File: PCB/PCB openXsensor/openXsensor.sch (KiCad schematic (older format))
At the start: 32 parts, among them P1 Digital, P10 VFAS/COURANT, P11 GY-86, P12 NTC1, P13 NTC2, P14 ALIM, P16 4S, P17 ADS1115, P18 ADS_IN, P2 Analog, P3 ADC, P4 ADC, P4-2 ADC, P5 GPS, P6 HUB/SPORT, P7 PPM, P8 FUEL, P9 RPM

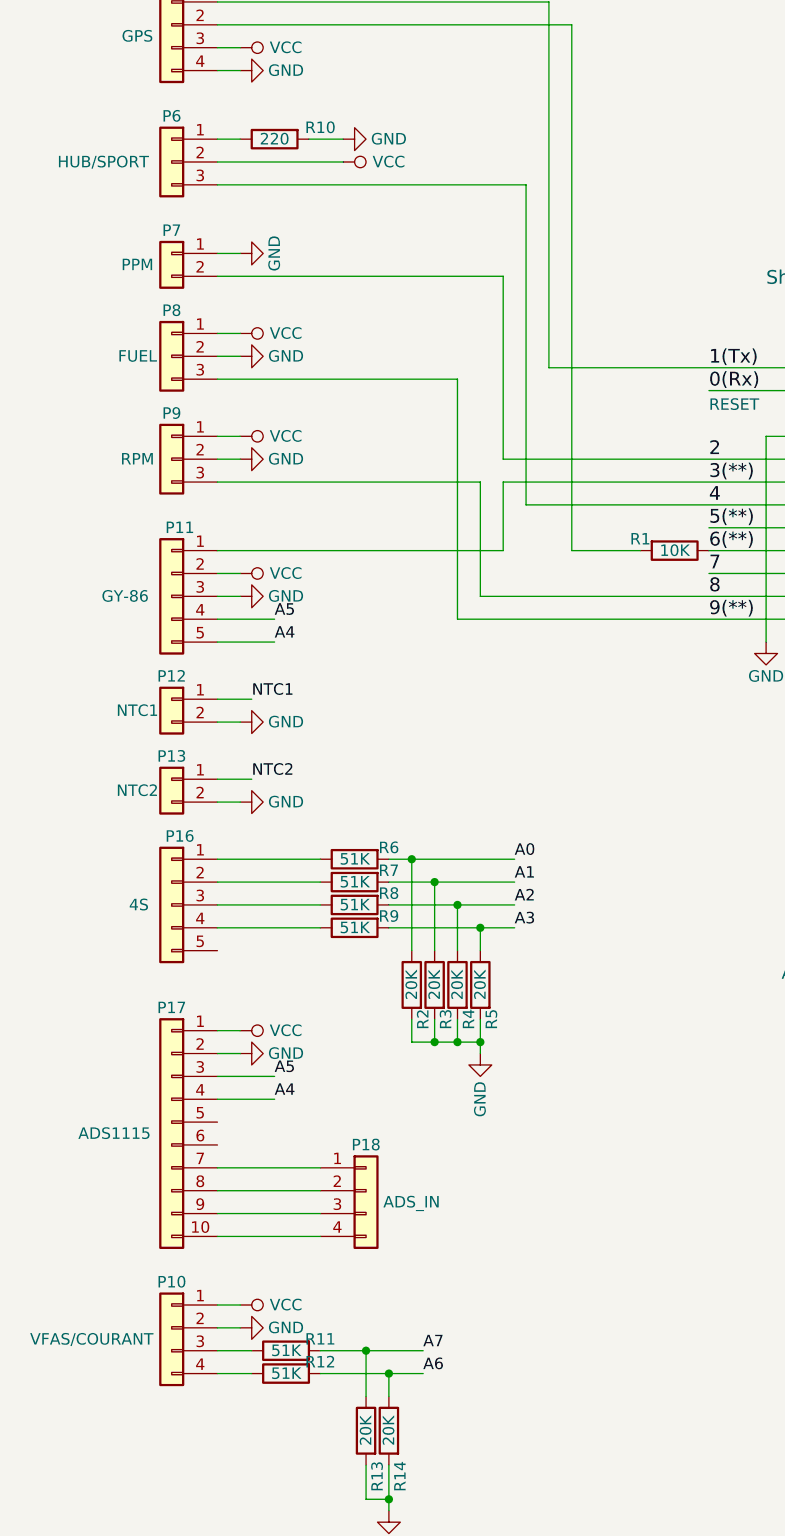
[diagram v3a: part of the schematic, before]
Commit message: Update oXs pcb
Move connectors p8 p9 under pro mini
Add connector between 5v and sport connector. 
Add gnd ads1115 addr pin (0x48).
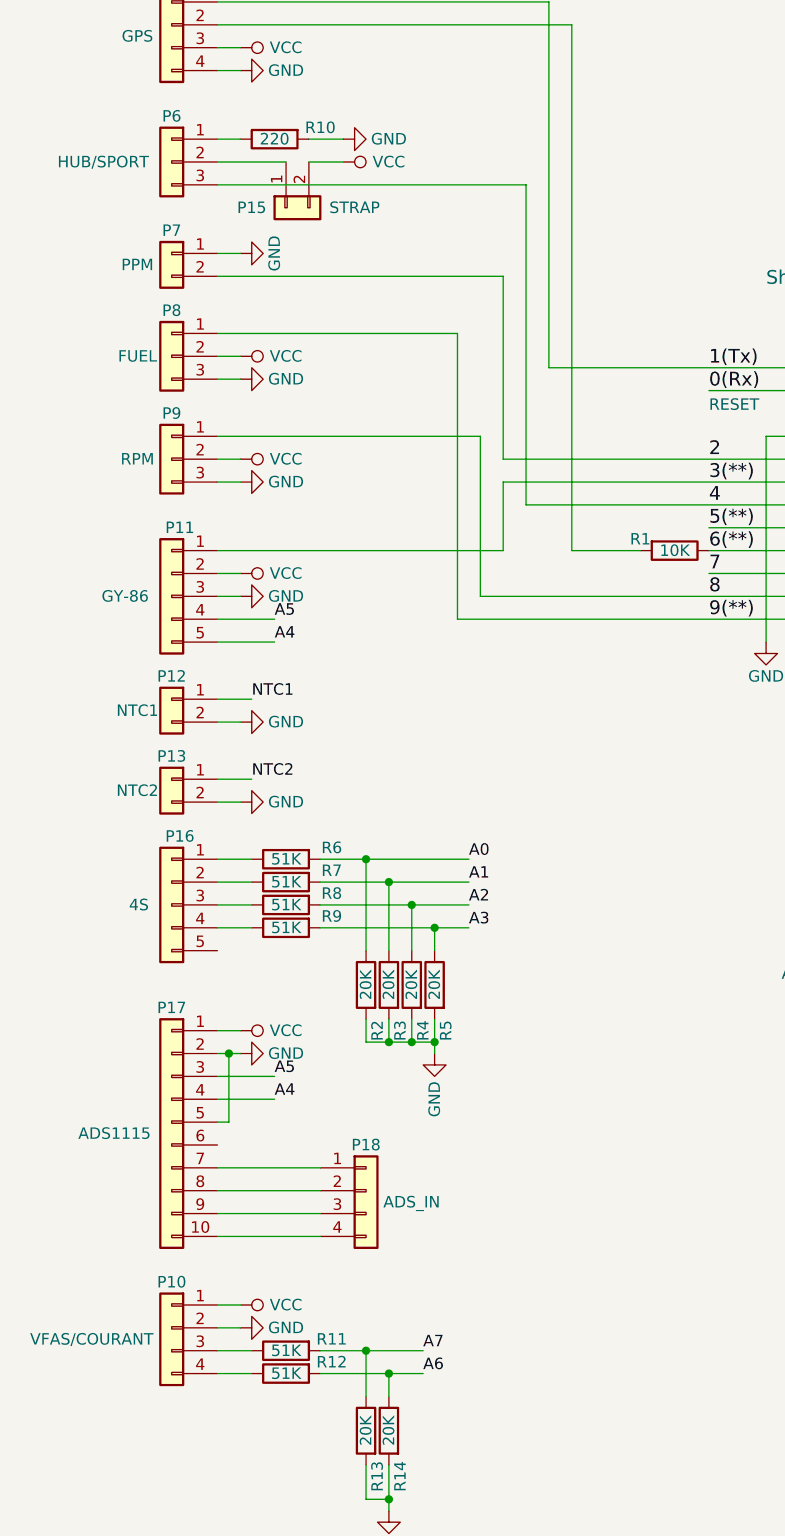
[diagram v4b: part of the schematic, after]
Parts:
- added P15: STRAP, Pin_Header_Straight_1x02_Pitch2.54mm, symbol Connector_Generic:Conn_01x02
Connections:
- net 8: now also P9.1 (Pin_1); no longer P9.3 (Pin_3)
- net 9(**): now also P8.1 (Pin_1); no longer P8.3 (Pin_3)
- net GND: now also P17.5 (Pin_5), P8.3 (Pin_3), P9.3 (Pin_3); no longer P8.2 (Pin_2), P9.2 (Pin_2)
- net VCC: now also P8.2 (Pin_2), P9.2 (Pin_2), P15.2 (Pin_2); no longer P6.2 (Pin_2), P8.1 (Pin_1), P9.1 (Pin_1)
- new net: P15.1 (Pin_1), P6.2 (Pin_2)
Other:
- moved on the sheet: R2, R3, R4, R5, R6, R7, R8, R9

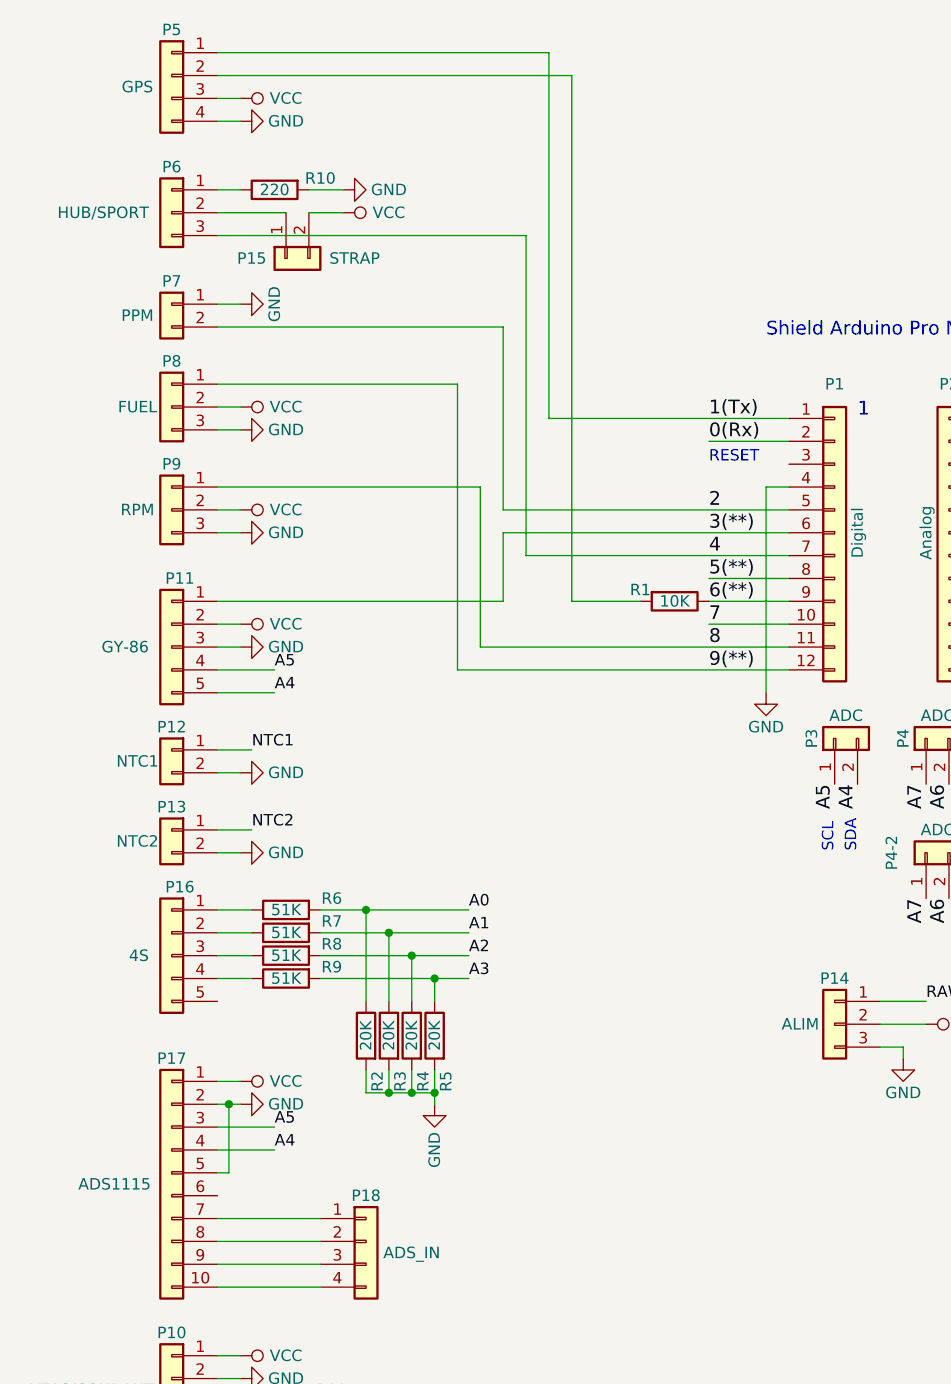
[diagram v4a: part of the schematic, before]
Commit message: Update pcb oxs
Change wire on gps connector
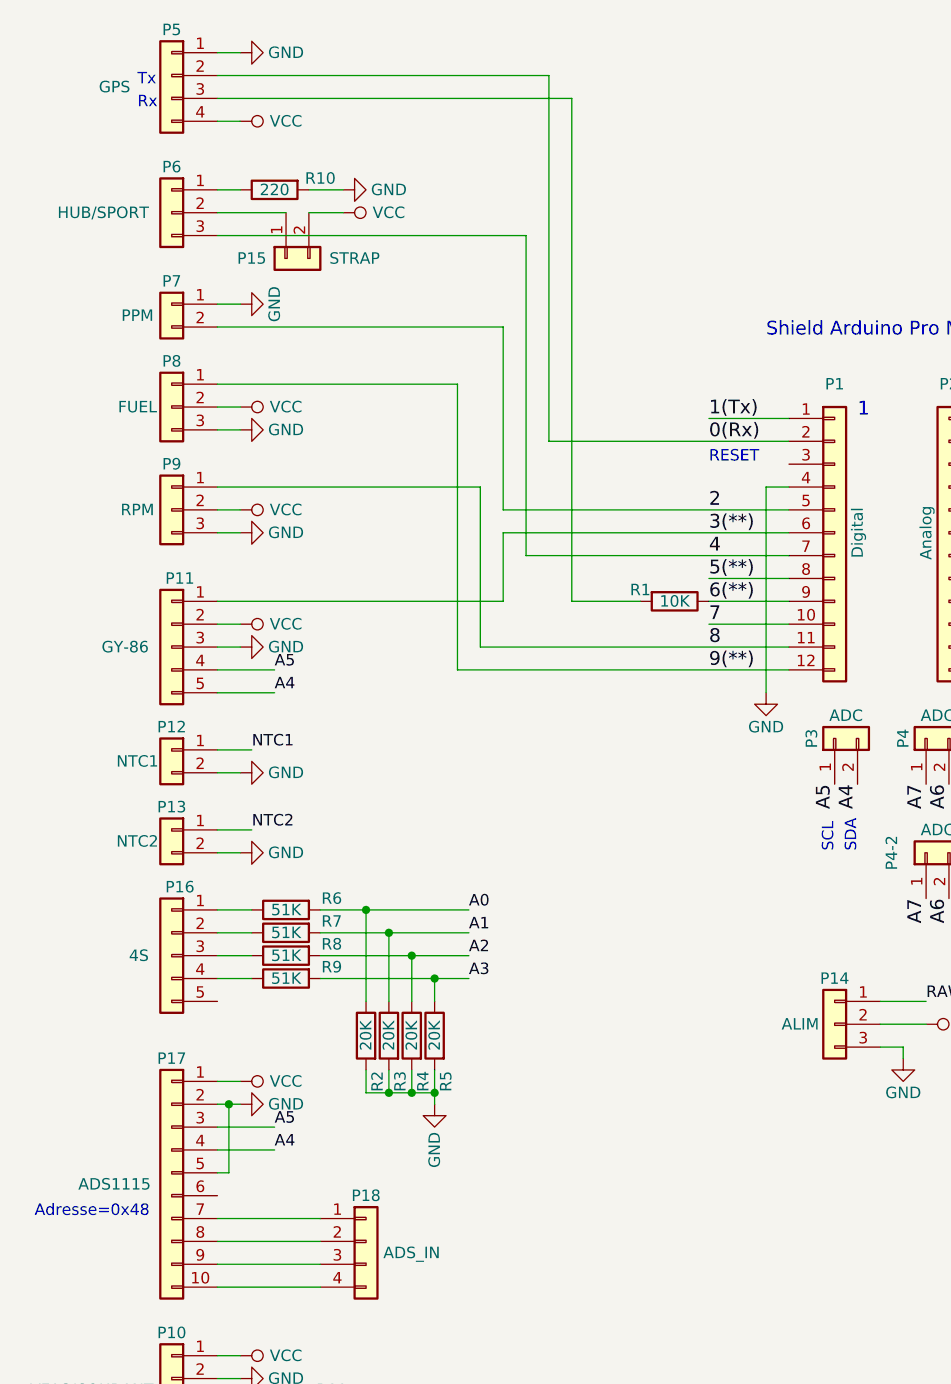
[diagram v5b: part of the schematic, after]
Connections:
- net 0(Rx): now also P5.2 (Pin_2)
- net 1(Tx): no longer P5.1 (Pin_1)
- net GND: now also P5.1 (Pin_1); no longer P5.4 (Pin_4)
- net VCC: now also P5.4 (Pin_4); no longer P5.3 (Pin_3)
- net at R1.2: now also P5.3 (Pin_3); no longer P5.2 (Pin_2)
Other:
- note added: "Adresse=0x48"
- note added: "Rx"
- note added: "Tx"
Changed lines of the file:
@@
 Sheet 1 1
 Title ""
-Date "2019-10-07"
+Date "2019-10-12"
 Rev ""
 Comp ""
@@
 	5450 2600 5450 3500
 Wire Wire Line
-	5200 2400 5550 2400
-Wire Wire Line
 	5200 3000 5550 3000
 Wire Wire Line
@@
 P 2850 800
 F 0 "P5" H 2850 1000 50  0000 C CNN
-F 1 "GPS" H 3000 750 50  0000 C CNN
+F 1 "GPS" H 3100 750 50  0000 C CNN
 F 2 "Pin_Header_Straight_1x04_Pitch2.54mm" H 2850 800 50  0001 C CNN
 F 3 "~" H 2850 800 50  0001 C CNN
@@
 	4900 3100 4600 3100
 Wire Wire Line
-	4600 3100 4600 800
-Wire Wire Line
-	4600 800  3050 800
-Wire Wire Line
-	4500 2300 5550 2300
-Wire Wire Line
-	3050 1000 3150 1000
+	4600 3100 4600 900
+Wire Wire Line
+	3050 700  3150 700
 $Comp
 L power:GND #PWR0101
 U 1 1 5D744512
-P 3150 1000
-F 0 "#PWR0101" H 3150 750 50  0001 C CNN
-F 1 "GND" V 3150 800 50  0000 C CNN
-F 2 "" H 3150 1000 50  0000 C CNN
-F 3 "" H 3150 1000 50  0000 C CNN
-	1    3150 1000
+P 3150 700
+F 0 "#PWR0101" H 3150 450 50  0001 C CNN
+F 1 "GND" V 3150 500 50  0000 C CNN
+F 2 "" H 3150 700 50  0000 C CNN
+F 3 "" H 3150 700 50  0000 C CNN
+	1    3150 700
 	0    -1   -1   0
 $EndComp
@@
 L power:VCC #PWR0104
 U 1 1 5D746203
-P 3150 900
-F 0 "#PWR0104" H 3150 750 50  0001 C CNN
-F 1 "VCC" V 3150 1100 50  0000 C CNN
-F 2 "" H 3150 900 50  0000 C CNN
-F 3 "" H 3150 900 50  0000 C CNN
-	1    3150 900
+P 3150 1000
+F 0 "#PWR0104" H 3150 850 50  0001 C CNN
+F 1 "VCC" V 3150 1200 50  0000 C CNN
+F 2 "" H 3150 1000 50  0000 C CNN
+F 3 "" H 3150 1000 50  0000 C CNN
+	1    3150 1000
 	0    1    1    0
 $EndComp
@@
 	3050 2800 3150 2800
 Wire Wire Line
-	3150 900  3050 900
-Wire Wire Line
-	4500 700  3050 700
+	3150 1000 3050 1000
 $Comp
 L Connector_Generic:Conn_01x04 P18
@@
 Wire Wire Line
 	4400 1500 4400 2900
-Wire Wire Line
-	4500 700  4500 2300
 $Comp
 L Device:R R14
@@
 Wire Wire Line
 	3100 5300 3050 5300
+Text Notes 2250 5800 0    50   ~ 0
+Adresse=0x48
+Text Notes 2700 950  0    50   ~ 0
+Rx
+Text Notes 2700 850  0    50   ~ 0
+Tx
+Wire Wire Line
+	5550 2300 5200 2300
+Wire Wire Line
+	4500 2400 5550 2400
+Wire Wire Line
+	4500 800  3050 800
+Wire Wire Line
+	4500 800  4500 2400
+Wire Wire Line
+	3050 900  4600 900
 $EndSCHEMATC

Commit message: Update oXs pcb
Add sequencer connector
Add capacitors on analog input 
Add capacitors on 5v and raw power 
...
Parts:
- removed P15: STRAP, Pin_Header_Straight_1x02_Pitch2.54mm, symbol Connector_Generic:Conn_01x02
- removed P4-2: ADC, Socket_Arduino_Pro_Mini:Socket_Strip_Arduino_1x02, symbol Connector_Generic:Conn_01x02
- removed R12: 51K, R_1206, symbol Device:R
- removed R13, R14: 20K, R_1206, symbol Device:R
- added C1, C10, C11, C14, C2, C3, C4, C7, C8, C9: 100nF, Empreintes:C_1206, symbol Device:C
- added C5, C6: 10uF, Empreintes:CP_EIA-3216-18_Kemet-A_Pad1.58x1.35mm_HandSolder, symbol Device:CP
- added P15: SEQUENCEUR, Empreintes:Pin_Header_Straight_1x04_Pitch2.54mm, symbol Connector_Generic:Conn_01x04
- added P19: MPXV7002DP, Empreintes:Pin_Header_Straight_1x03_Pitch2.54mm, symbol Connector_Generic:Conn_01x03
- P10, P5: footprint Pin_Header_Straight_1x04_Pitch2.54mm -> Empreintes:Pin_Header_Straight_1x04_Pitch2.54mm
- P11, P16: footprint Pin_Header_Straight_1x05_Pitch2.54mm -> Empreintes:Pin_Header_Straight_1x05_Pitch2.54mm
- P12, P13, P7: footprint Pin_Header_Straight_1x02_Pitch2.54mm -> Empreintes:Pin_Header_Straight_1x02_Pitch2.54mm
- P14, P6, P8, P9: footprint Pin_Header_Straight_1x03_Pitch2.54mm -> Empreintes:Pin_Header_Straight_1x03_Pitch2.54mm
- P17: footprint Pin_Header_Straight_1x10_Pitch2.54mm -> Empreintes:Pin_Header_Straight_1x10_Pitch2.54mm
- P18: value ADS_IN -> MS4525DO; footprint Pin_Header_Straight_1x04_Pitch2.54mm -> Empreintes:Pin_Header_Straight_1x04_Pitch2.54mm
- R1, R10, R2, R3, R4, R5, R6, R7, R8, R9: footprint R_1206 -> Empreintes:R_1206
- R11: value 51K -> 0; footprint R_1206 -> Empreintes:R_1206
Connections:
- net NTC1 is gone; now on net A6: P12.1 (Pin_1)
- net NTC2 is gone; now on net A7: P13.1 (Pin_1)
- net A0: now also C1.1
- net A1: now also C2.1
- net A2: now also C3.1
- net A3: now also C4.1
- net A4: now also P18.3 (Pin_3)
- net A5: now also P18.2 (Pin_2)
- net A6: now also C10.1
- net A7: now also C11.1; no longer R11.2
- net GND: now also P18.4 (Pin_4), C1.2, C10.2, C11.2, C14.2, C2.2, C3.2, C4.2, C5.2, C6.2, C7.2, C8.2, C9.2, P19.2 (Pin_2)
- net RAW: now also C5.1
- net VCC: now also P18.1 (Pin_1), R11.2, C6.1, P19.1 (Pin_1)
- net at R11.1: now also P6.2 (Pin_2); no longer P10.3 (Pin_3)
- net ADS_VOLT2: now reaches P10.4 (Pin_4)
- net ADS_VOLT2: now also P17.8 (Pin_8), C9.1
- net ADS_VOLT4: now reaches P17.10 (Pin_10)
- net ADS_VOLT4: now also P8.1 (Pin_1), C14.1; no longer P18.4 (Pin_4)
- net ADS_VOLT1: now reaches P17.7 (Pin_7)
- net ADS_VOLT1: now also P10.3 (Pin_3), C8.1; no longer P18.1 (Pin_1)
- net ADS_VOLT3: now reaches P17.9 (Pin_9)
- net ADS_VOLT3: now also C7.1, P19.3 (Pin_3); no longer P18.3 (Pin_3)
- net 10(**/SS) renamed SEQ2
- net SEQ2: now also P15.3 (Pin_3)
- net 11(**/MOSI) renamed SEQ3
- net SEQ3: now also P15.2 (Pin_2)
- net 12(MISO) renamed SEQ4
- net SEQ4: now also P15.1 (Pin_1)
- net 9(**) renamed SEQ1
- net SEQ1: now also P15.4 (Pin_4); no longer P8.1 (Pin_1)
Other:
- note added: "(0x48)"
- note added: "COURANT"
- note added: "STRAP"
- note added: "VFAS"
- note added: "VSPEED(ANALOG)"
- note added: "VSPEED(I2C)"
- note removed: "Adresse=0x48"
- moved on the sheet: P1, P10, P11, P12, P13, P14, P16, P17, P2, P3, P4, P5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
